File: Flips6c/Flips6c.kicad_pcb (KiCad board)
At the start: 2 copper layers, 100 x 50 mm, 24 parts, among them CN1 Conn_02x04_Odd_Even, U1 74595, U2 74595, U3 74595

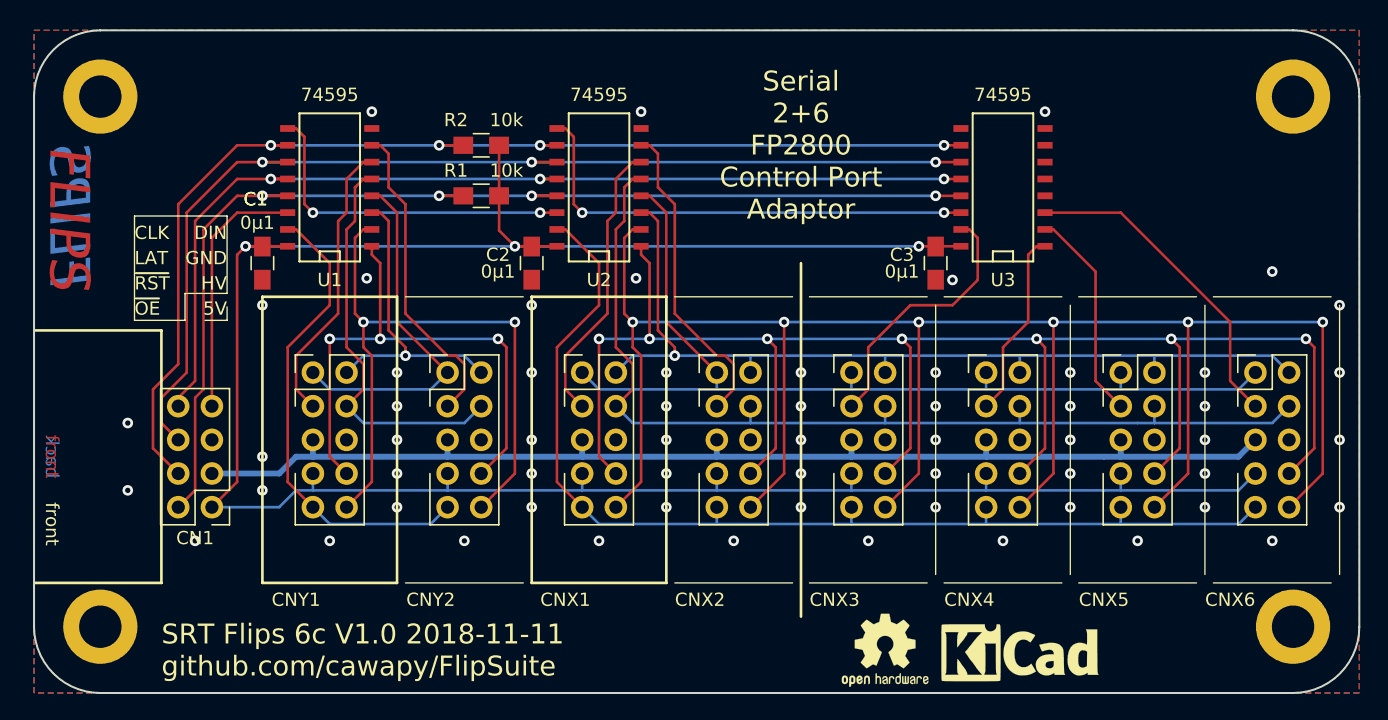
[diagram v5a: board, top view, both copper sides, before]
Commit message: allign grid origin to upper left corner
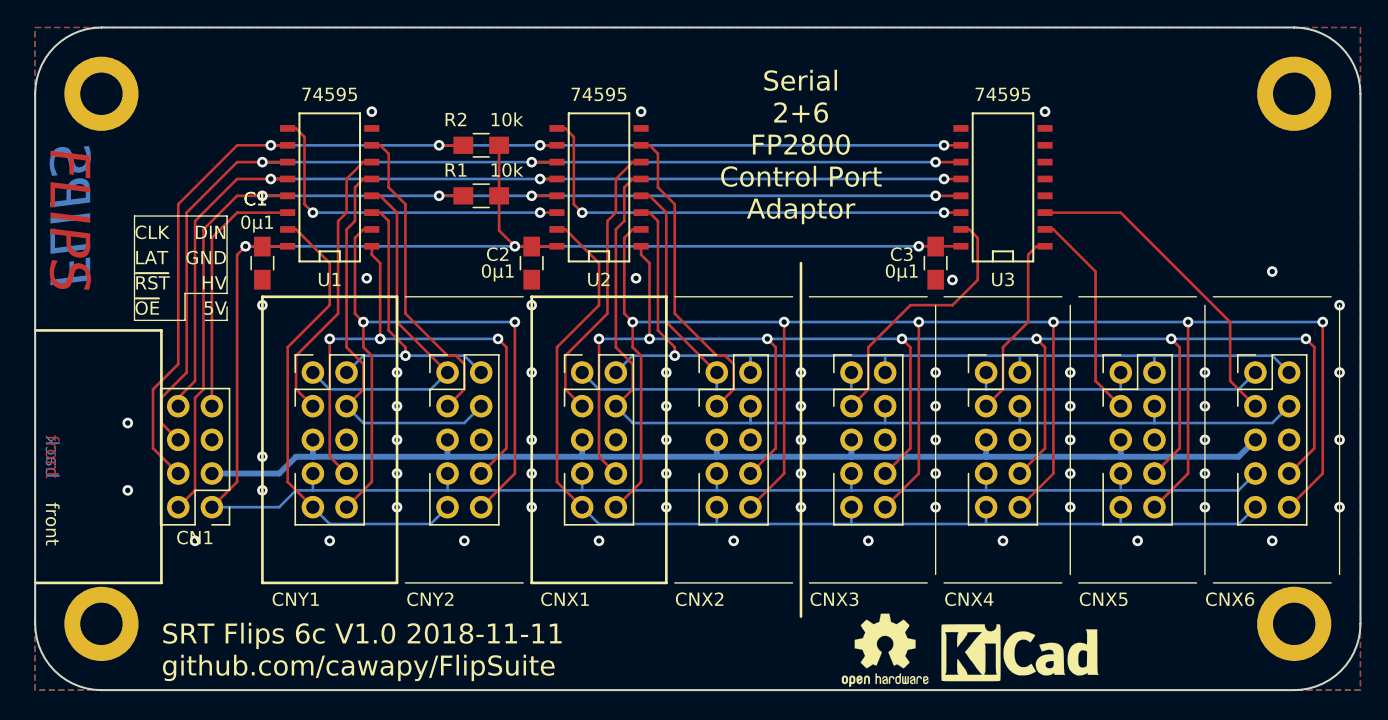
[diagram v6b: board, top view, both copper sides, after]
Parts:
- moved REF** 0.23 mm to (177.1, 102.8)
- moved REF** 0.23 mm to (177.1, 62.8)
- moved REF** 0.23 mm to (267.1, 102.8)
- moved REF** 0.23 mm to (267.1, 62.8)
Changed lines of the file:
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@@
   (page A4)
   (layers
-    (0 F.Cu signal hide)
+    (0 F.Cu signal)
     (31 B.Cu signal)
     (32 B.Adhes user)
@@
     (solder_mask_min_width 0.25)
     (aux_axis_origin 0 0)
+    (grid_origin 172.085 57.785)
     (visible_elements 7FFFFFFF)
     (pcbplotparams
@@
   )
   (module Mounting_Holes:MountingHole_3.2mm_M3_DIN965_Pad (layer F.Cu)
-    (at 177 103)
+    (at 177.085 102.785)
     (descr "Mounting Hole 3.2mm, M3, DIN965")
     (tags "mounting hole 3.2mm m3 din965")
@@
   )
   (module Mounting_Holes:MountingHole_3.2mm_M3_DIN965_Pad (layer F.Cu)
-    (at 267 103)
+    (at 267.085 102.785)
     (descr "Mounting Hole 3.2mm, M3, DIN965")
     (tags "mounting hole 3.2mm m3 din965")
@@
   )
   (module Mounting_Holes:MountingHole_3.2mm_M3_DIN965_Pad (layer F.Cu)
-    (at 267 63)
+    (at 267.085 62.785)
     (descr "Mounting Hole 3.2mm, M3, DIN965")
     (tags "mounting hole 3.2mm m3 din965")
@@
   )
   (module Mounting_Holes:MountingHole_3.2mm_M3_DIN965_Pad (layer F.Cu)
-    (at 177 63)
+    (at 177.085 62.785)
     (descr "Mounting Hole 3.2mm, M3, DIN965")
     (tags "mounting hole 3.2mm m3 din965")
@@
   (gr_line (start 189.23 80.645) (end 179.07 80.645) (layer Margin) (width 0.2))
   (dimension 100 (width 0.3) (layer Dwgs.User)
-    (gr_text "100,000 mm" (at 222 36.9) (layer Dwgs.User)
+    (gr_text "100,000 mm" (at 222.085 36.685) (layer Dwgs.User)
       (effects (font (size 1.5 1.5) (thickness 0.3)))
     )
-    (feature1 (pts (xy 172 56) (xy 172 38.413579)))
-    (feature2 (pts (xy 272 56) (xy 272 38.413579)))
-    (crossbar (pts (xy 272 39) (xy 172 39)))
-    (arrow1a (pts (xy 172 39) (xy 173.126504 38.413579)))
-    (arrow1b (pts (xy 172 39) (xy 173.126504 39.586421)))
-    (arrow2a (pts (xy 272 39) (xy 270.873496 38.413579)))
-    (arrow2b (pts (xy 272 39) (xy 270.873496 39.586421)))
+    (feature1 (pts (xy 172.085 55.785) (xy 172.085 38.198579)))
+    (feature2 (pts (xy 272.085 55.785) (xy 272.085 38.198579)))
+    (crossbar (pts (xy 272.085 38.785) (xy 172.085 38.785)))
+    (arrow1a (pts (xy 172.085 38.785) (xy 173.211504 38.198579)))
+    (arrow1b (pts (xy 172.085 38.785) (xy 173.211504 39.371421)))
+    (arrow2a (pts (xy 272.085 38.785) (xy 270.958496 38.198579)))
+    (arrow2b (pts (xy 272.085 38.785) (xy 270.958496 39.371421)))
   )
   (dimension 90 (width 0.3) (layer Dwgs.User)
-    (gr_text "90,000 mm" (at 222 44.9) (layer Dwgs.User)
+    (gr_text "90,000 mm" (at 222.085 44.685) (layer Dwgs.User)
       (effects (font (size 1.5 1.5) (thickness 0.3)))
     )
-    (feature1 (pts (xy 177 56) (xy 177 46.413579)))
-    (feature2 (pts (xy 267 56) (xy 267 46.413579)))
-    (crossbar (pts (xy 267 47) (xy 177 47)))
-    (arrow1a (pts (xy 177 47) (xy 178.126504 46.413579)))
-    (arrow1b (pts (xy 177 47) (xy 178.126504 47.586421)))
-    (arrow2a (pts (xy 267 47) (xy 265.873496 46.413579)))
-    (arrow2b (pts (xy 267 47) (xy 265.873496 47.586421)))
+    (feature1 (pts (xy 177.085 55.785) (xy 177.085 46.198579)))
+    (feature2 (pts (xy 267.085 55.785) (xy 267.085 46.198579)))
+    (crossbar (pts (xy 267.085 46.785) (xy 177.085 46.785)))
+    (arrow1a (pts (xy 177.085 46.785) (xy 178.211504 46.198579)))
+    (arrow1b (pts (xy 177.085 46.785) (xy 178.211504 47.371421)))
+    (arrow2a (pts (xy 267.085 46.785) (xy 265.958496 46.198579)))
+    (arrow2b (pts (xy 267.085 46.785) (xy 265.958496 47.371421)))
   )
   (dimension 40 (width 0.3) (layer Dwgs.User)
-    (gr_text "40,000 mm" (at 286.1 83 90) (layer Dwgs.User)
+    (gr_text "40,000 mm" (at 286.185 82.785 90) (layer Dwgs.User)
       (effects (font (size 1.5 1.5) (thickness 0.3)))
     )
-    (feature1 (pts (xy 274 63) (xy 284.586421 63)))
-    (feature2 (pts (xy 274 103) (xy 284.586421 103)))
-    (crossbar (pts (xy 284 103) (xy 284 63)))
-    (arrow1a (pts (xy 284 63) (xy 284.586421 64.126504)))
-    (arrow1b (pts (xy 284 63) (xy 283.413579 64.126504)))
-    (arrow2a (pts (xy 284 103) (xy 284.586421 101.873496)))
-    (arrow2b (pts (xy 284 103) (xy 283.413579 101.873496)))
+    (feature1 (pts (xy 274.085 62.785) (xy 284.671421 62.785)))
+    (feature2 (pts (xy 274.085 102.785) (xy 284.671421 102.785)))
+    (crossbar (pts (xy 284.085 102.785) (xy 284.085 62.785)))
+    (arrow1a (pts (xy 284.085 62.785) (xy 284.671421 63.911504)))
+    (arrow1b (pts (xy 284.085 62.785) (xy 283.498579 63.911504)))
+    (arrow2a (pts (xy 284.085 102.785) (xy 284.671421 101.658496)))
+    (arrow2b (pts (xy 284.085 102.785) (xy 283.498579 101.658496)))
   )
   (dimension 50 (width 0.3) (layer Dwgs.User)
-    (gr_text "50,000 mm" (at 292.1 83 90) (layer Dwgs.User)
+    (gr_text "50,000 mm" (at 292.185 82.785 90) (layer Dwgs.User)
       (effects (font (size 1.5 1.5) (thickness 0.3)))
     )
-    (feature1 (pts (xy 274 58) (xy 290.586421 58)))
-    (feature2 (pts (xy 274 108) (xy 290.586421 108)))
-    (crossbar (pts (xy 290 108) (xy 290 58)))
-    (arrow1a (pts (xy 290 58) (xy 290.586421 59.126504)))
-    (arrow1b (pts (xy 290 58) (xy 289.413579 59.126504)))
-    (arrow2a (pts (xy 290 108) (xy 290.586421 106.873496)))
-    (arrow2b (pts (xy 290 108) (xy 289.413579 106.873496)))
-  )
-  (gr_arc (start 177 103) (end 172 103) (angle -90) (layer Edge.Cuts) (width 0.15))
-  (gr_arc (start 177 63) (end 177 58) (angle -90) (layer Edge.Cuts) (width 0.15))
-  (gr_arc (start 267 63) (end 272 63) (angle -90) (layer Edge.Cuts) (width 0.15))
-  (gr_arc (start 267 103) (end 267 108) (angle -90) (layer Edge.Cuts) (width 0.15))
-  (gr_line (start 272 63) (end 272 103) (layer Edge.Cuts) (width 0.15))
-  (gr_line (start 177 58) (end 267 58) (layer Edge.Cuts) (width 0.15))
-  (gr_line (start 172 103) (end 172 63) (layer Edge.Cuts) (width 0.15))
-  (gr_line (start 267 108) (end 177 108) (layer Edge.Cuts) (width 0.15))
+    (feature1 (pts (xy 274.085 57.785) (xy 290.671421 57.785)))
+    (feature2 (pts (xy 274.085 107.785) (xy 290.671421 107.785)))
+    (crossbar (pts (xy 290.085 107.785) (xy 290.085 57.785)))
+    (arrow1a (pts (xy 290.085 57.785) (xy 290.671421 58.911504)))
+    (arrow1b (pts (xy 290.085 57.785) (xy 289.498579 58.911504)))
+    (arrow2a (pts (xy 290.085 107.785) (xy 290.671421 106.658496)))
+    (arrow2b (pts (xy 290.085 107.785) (xy 289.498579 106.658496)))
+  )
+  (gr_arc (start 177.085 102.785) (end 172.085 102.785) (angle -90) (layer Edge.Cuts) (width 0.15))
+  (gr_arc (start 177.085 62.785) (end 177.085 57.785) (angle -90) (layer Edge.Cuts) (width 0.15))
+  (gr_arc (start 267.085 62.785) (end 272.085 62.785) (angle -90) (layer Edge.Cuts) (width 0.15))
+  (gr_arc (start 267.085 102.785) (end 267.085 107.785) (angle -90) (layer Edge.Cuts) (width 0.15))
+  (gr_line (start 272.085 62.785) (end 272.085 102.785) (layer Edge.Cuts) (width 0.15))
+  (gr_line (start 177.085 57.785) (end 267.085 57.785) (layer Edge.Cuts) (width 0.15))
+  (gr_line (start 172.085 102.785) (end 172.085 62.785) (layer Edge.Cuts) (width 0.15))
+  (gr_line (start 267.085 107.785) (end 177.085 107.785) (layer Edge.Cuts) (width 0.15))
   (gr_line (start 189.23 78.105) (end 260.35 78.105) (layer Margin) (width 0.2))
   (gr_line (start 189.23 99.695) (end 189.23 78.105) (layer Margin) (width 0.2))
@@
     (polygon
       (pts
-        (xy 172 58) (xy 272 58) (xy 272 108) (xy 172 108)
+        (xy 172.085 57.785) (xy 272.085 57.785) (xy 272.085 107.785) (xy 172.085 107.785)
       )
     )
@@
     (polygon
       (pts
-        (xy 272 58) (xy 272 108) (xy 172 108) (xy 172 58)
+        (xy 272.085 57.785) (xy 272.085 107.785) (xy 172.085 107.785) (xy 172.085 57.785)
       )
     )

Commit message: adding logo
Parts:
- added REF**: FlipsLogo-Mittel, Own:FlipsLogo-Mittel, F.Cu at (185.4, 105.4)
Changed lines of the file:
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@@
     (tracks 454)
     (zones 0)
-    (modules 24)
+    (modules 25)
     (nets 36)
   )
@@
     )
   )
+  (module Own:FlipsLogo-Mittel (layer F.Cu)
+    (at 185.42 105.41)
+    (fp_text reference REF** (at 0 3.81) (layer F.Fab) hide
+      (effects (font (size 1 1) (thickness 0.15)))
+    )
+    (fp_text value FlipsLogo-Mittel (at 0 2.54) (layer F.Fab)
+      (effects (font (size 1 1) (thickness 0.15)))
+    )
+    (fp_line (start -0.381 0) (end -0.6985 -0.3175) (layer F.SilkS) (width 0.2))
+    (fp_line (start -3.048 -2.667) (end -2.7178 -2.3368) (layer F.SilkS) (width 0.2))
+    (fp_line (start -3.048 1.778) (end -3.048 -2.667) (layer F.CrtYd) (width 0.1))
+    (fp_line (start 3.048 1.778) (end -3.048 1.778) (layer F.CrtYd) (width 0.1))
+    (fp_line (start 3.048 -2.667) (end 3.048 1.778) (layer F.CrtYd) (width 0.1))
+    (fp_line (start -3.048 -2.667) (end 3.048 -2.667) (layer F.CrtYd) (width 0.1))
+    (fp_poly (pts (xy -0.381 -1.905) (xy -0.381 -0.762) (xy -1.143 0) (xy -2.286 0)
+      (xy -3.048 -0.762) (xy -3.048 -1.905) (xy -2.286 -2.667) (xy -1.143 -2.667)) (layer F.SilkS) (width 0.15))
+    (fp_line (start 0.381 -2.667) (end 0.7112 -2.3368) (layer F.SilkS) (width 0.2))
+    (fp_line (start 1.143 0) (end 2.286 0) (layer F.SilkS) (width 0.1))
+    (fp_line (start 0.381 -0.762) (end 1.143 0) (layer F.SilkS) (width 0.1))
+    (fp_line (start 0.381 -1.905) (end 0.381 -0.762) (layer F.SilkS) (width 0.1))
+    (fp_line (start 1.143 -2.667) (end 0.381 -1.905) (layer F.SilkS) (width 0.1))
+    (fp_line (start 2.159 -2.667) (end 1.143 -2.667) (layer F.SilkS) (width 0.1))
+    (fp_line (start 3.048 -1.905) (end 2.286 -2.667) (layer F.SilkS) (width 0.1))
+    (fp_line (start 3.048 -0.762) (end 3.048 -1.905) (layer F.SilkS) (width 0.1))
+    (fp_line (start 2.286 0) (end 3.048 -0.762) (layer F.SilkS) (width 0.1))
+    (fp_line (start 3.048 0) (end 2.7305 -0.3175) (layer F.SilkS) (width 0.2))
+    (fp_text user FLIPS (at 0 1.016) (layer F.SilkS)
+      (effects (font (size 1 1) (thickness 0.2) italic))
+    )
+  )
   (gr_line (start 260.985 78.105) (end 269.875 78.105) (layer F.SilkS) (width 0.1))
   (gr_line (start 270.51 78.74) (end 270.51 99.06) (layer F.SilkS) (width 0.1))
@@
   (gr_line (start 230.505 78.105) (end 239.395 78.105) (layer F.SilkS) (width 0.1))
   (gr_line (start 240.665 78.105) (end 249.555 78.105) (layer F.SilkS) (width 0.1))
-  (gr_text "SRT Flips 6c V1.0 2018-11-11\ngithub.com/cawapy/FlipSuite" (at 181.61 104.775) (layer F.SilkS)
+  (gr_text "SRT Flips 6c V1.0 2018-11-11\ngithub.com/cawapy/FlipSuite" (at 190.5 104.775) (layer F.SilkS)
     (effects (font (size 1.5 1.5) (thickness 0.3)) (justify left))
   )

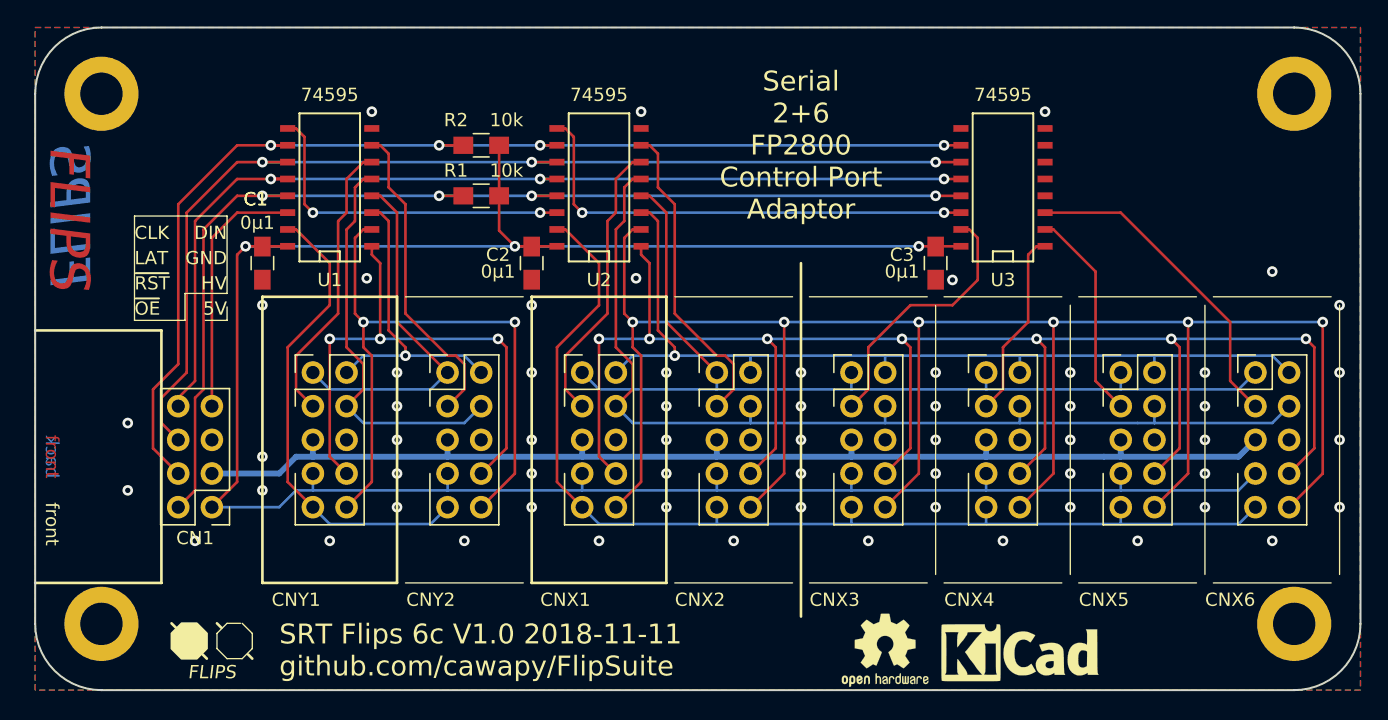
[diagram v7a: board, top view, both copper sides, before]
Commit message: improve trace spacing
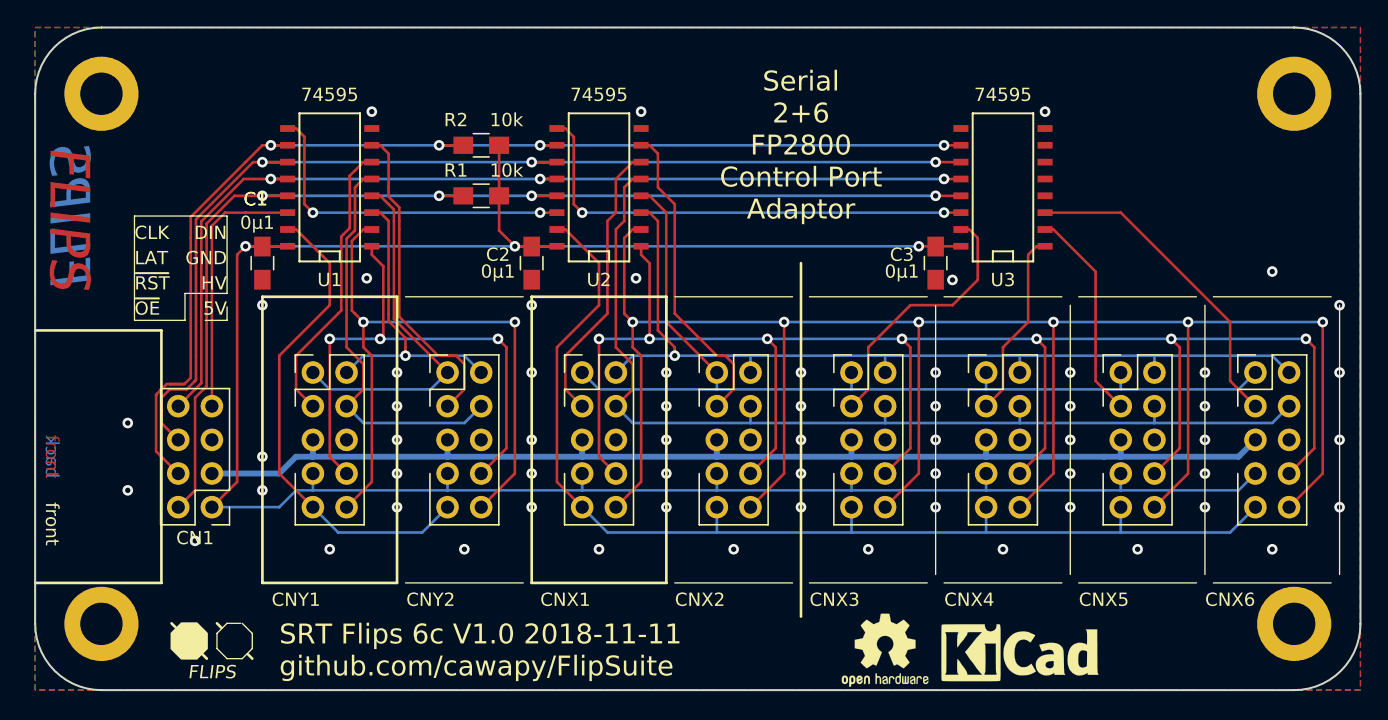
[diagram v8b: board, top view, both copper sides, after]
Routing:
- net /XA.0: track 81.7 -> 84.7 mm
- net /YA.0: track 36.0 -> 37.0 mm
- net /~SRCLR: track 88.4 -> 87.7 mm
- net /DIN: track 19.2 -> 19.7 mm
